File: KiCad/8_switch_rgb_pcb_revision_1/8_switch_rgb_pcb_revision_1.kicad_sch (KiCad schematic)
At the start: 95 parts, among them SW0 SW0, SW1 SW1, SW2 SW2, SW3 SW3, SW4 SW4, SW5 SW5, SW6 SW6, SW7 SW7, U2 74HC165, Y1 16MHz

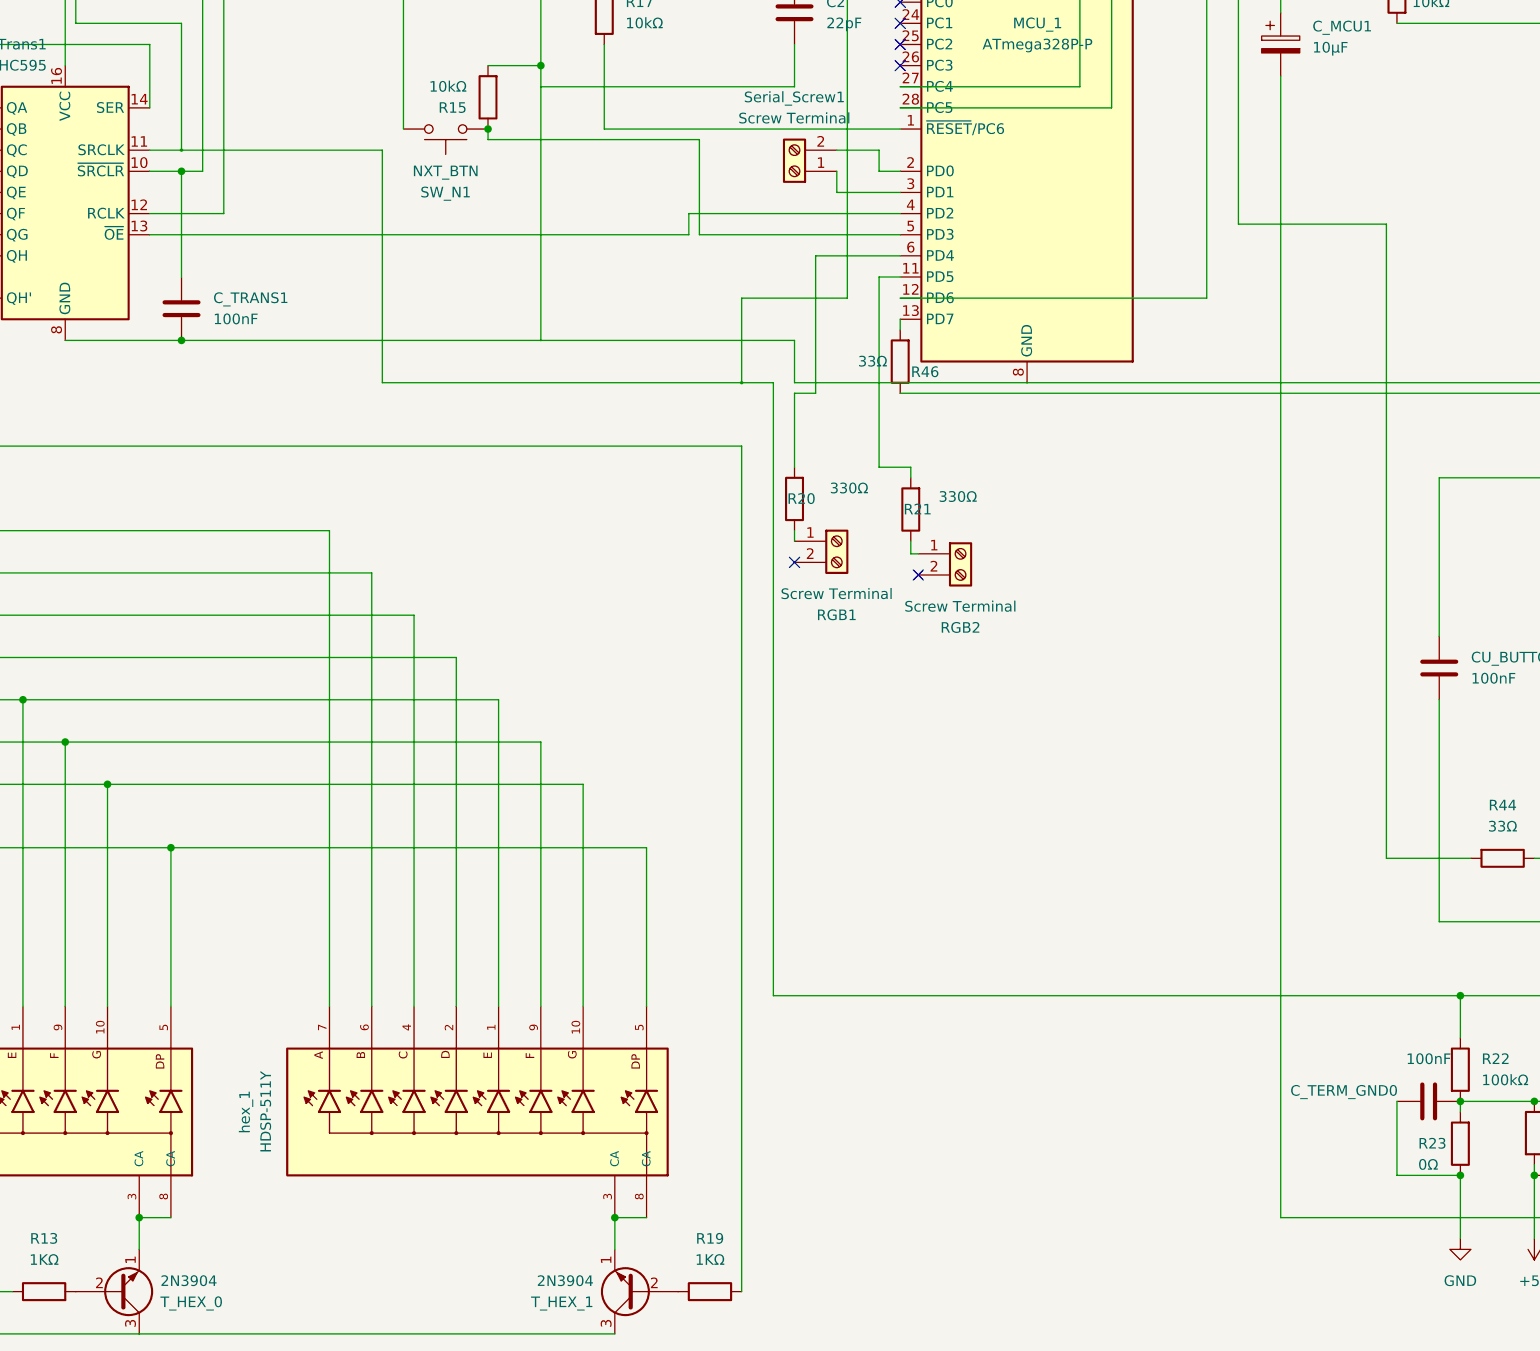
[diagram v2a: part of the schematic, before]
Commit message: Connected all traces. Will now run DRC This is the last 2-layer board with more than 10 components I ever create.
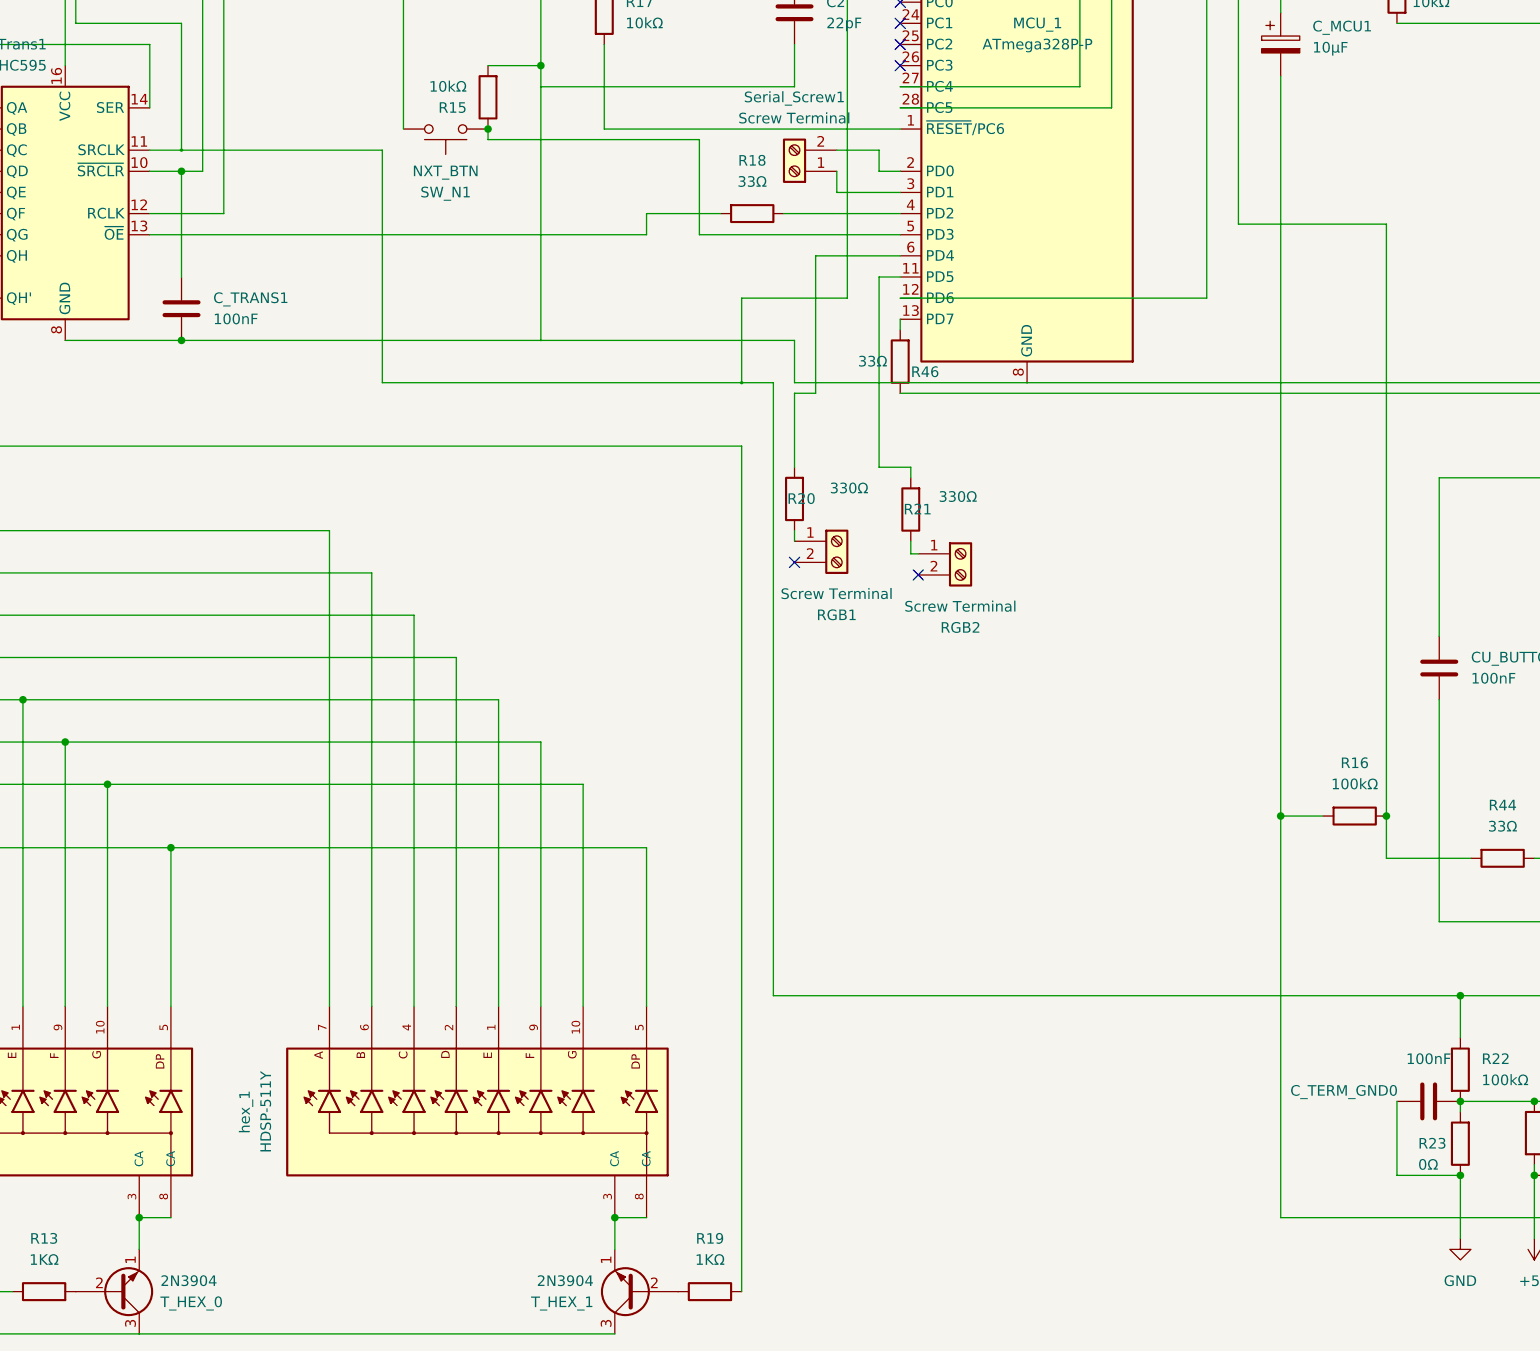
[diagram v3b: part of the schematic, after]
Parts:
- added R16: 100kΩ, Resistor_THT:R_Axial_DIN0204_L3.6mm_D1.6mm_P5.08mm_Horizontal, symbol Device:R
- added R18: 33Ω, Resistor_THT:R_Axial_DIN0204_L3.6mm_D1.6mm_P5.08mm_Horizontal, symbol Device:R
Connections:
- net GND: now also R16.2
- net at U_Trans1.13 (~{OE}): now also R18.2; no longer MCU_1.4 (PD2)
- net at MCU_1.18 (PB4), R44.2: now also R16.1
- new net: MCU_1.4 (PD2), R18.1
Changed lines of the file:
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@@
   (junction (at 134.62 170.18) (diameter 0) (color 0 0 0 0)
   )
+  (junction (at 303.53 189.23) (diameter 0) (color 0 0 0 0)
+  )
   (junction (at 66.04 165.1) (diameter 0) (color 0 0 0 0)
   )
@@
   (junction (at 398.78 175.26) (diameter 0.2) (color 0 0 0 1)
   )
+  (junction (at 290.83 189.23) (diameter 0) (color 0 0 0 0)
+  )
   (junction (at 321.31 223.52) (diameter 0) (color 0 0 0 0)
   )
@@
     (stroke (width 0) (type default))
   )
+  (wire (pts (xy 303.53 189.23) (xy 303.53 118.11))
+    (stroke (width 0) (type default))
+  )
   (wire (pts (xy 67.31 139.7) (xy 67.31 170.18))
     (stroke (width 0) (type default))
@@
     (stroke (width 0) (type default))
   )
+  (wire (pts (xy 290.83 189.23) (xy 290.83 237.49))
+    (stroke (width 0.2) (type default) (color 0 0 0 1))
+  )
   (wire (pts (xy 123.19 144.78) (xy 226.06 144.78))
     (stroke (width 0) (type default))
@@
     (stroke (width 0.2) (type default) (color 0 0 0 1))
   )
+  (wire (pts (xy 290.83 189.23) (xy 295.91 189.23))
+    (stroke (width 0.2) (type default) (color 0 0 0 1))
+  )
   (wire (pts (xy 382.27 152.4) (xy 398.78 152.4))
     (stroke (width 0.2) (type default) (color 0 0 0 1))
@@
     (stroke (width 0) (type default))
   )
-  (wire (pts (xy 303.53 194.31) (xy 303.53 118.11))
+  (wire (pts (xy 303.53 194.31) (xy 303.53 189.23))
     (stroke (width 0) (type default))
   )
@@
     (stroke (width 0.2) (type default) (color 255 0 0 1))
   )
+  (wire (pts (xy 231.14 116.84) (xy 245.11 116.84))
+    (stroke (width 0) (type default))
+  )
   (wire (pts (xy 367.03 87.63) (xy 367.03 82.55))
     (stroke (width 0) (type default))
@@
     (stroke (width 0.2) (type default) (color 255 0 0 1))
   )
-  (wire (pts (xy 219.71 116.84) (xy 245.11 116.84))
+  (wire (pts (xy 214.63 116.84) (xy 223.52 116.84))
     (stroke (width 0) (type default))
   )
@@
     (stroke (width 0) (type default))
   )
-  (wire (pts (xy 290.83 137.16) (xy 290.83 237.49))
+  (wire (pts (xy 290.83 137.16) (xy 290.83 189.23))
     (stroke (width 0.2) (type default) (color 0 0 0 1))
   )
@@
     (stroke (width 0.2) (type default) (color 255 0 0 1))
   )
-  (wire (pts (xy 219.71 119.38) (xy 219.71 116.84))
+  (wire (pts (xy 214.63 119.38) (xy 214.63 116.84))
     (stroke (width 0) (type default))
   )
@@
     (stroke (width 0) (type default))
   )
-  (wire (pts (xy 154.94 119.38) (xy 219.71 119.38))
+  (wire (pts (xy 154.94 119.38) (xy 214.63 119.38))
     (stroke (width 0) (type default))
   )
@@
     )
   )
+  (symbol (lib_id "Device:R") (at 299.72 189.23 270) (unit 1)
+    (in_bom yes) (on_board yes) (dnp no) (fields_autoplaced)
+    (property "Reference" "R16" (at 299.72 182.88 90)
+      (effects (font (size 1.27 1.27)))
+    )
+    (property "Value" "100kΩ" (at 299.72 185.42 90)
+      (effects (font (size 1.27 1.27)))
+    )
+    (property "Footprint" "Resistor_THT:R_Axial_DIN0204_L3.6mm_D1.6mm_P5.08mm_Horizontal" (at 299.72 187.452 90)
+      (effects (font (size 1.27 1.27)) hide)
+    )
+    (property "Datasheet" "~" (at 299.72 189.23 0)
+      (effects (font (size 1.27 1.27)) hide)
+    )
+    (pin "1")
+    (pin "2")
+    (instances
+      (project "8_switch_rgb_pcb_revision_1"
+        (path "/cd17c5d7-b2e9-44f9-9f0c-42378b59d72a"
+          (reference "R16") (unit 1)
+        )
+      )
+    )
+  )
   (symbol (lib_id "power:GND") (at 349.25 194.31 0) (unit 1)
     (in_bom yes) (on_board yes) (dnp no) (fields_autoplaced)
@@
         )
       )
+    )
+  )
+  (symbol (lib_id "Device:R") (at 227.33 116.84 270) (unit 1)
+    (in_bom yes) (on_board yes) (dnp no) (fields_autoplaced)
+    (property "Reference" "R18" (at 227.33 110.49 90)
+      (effects (font (size 1.27 1.27)))
+    )
+    (property "Value" "33Ω" (at 227.33 113.03 90)
+      (effects (font (size 1.27 1.27)))
+    )
+    (property "Footprint" "Resistor_THT:R_Axial_DIN0204_L3.6mm_D1.6mm_P5.08mm_Horizontal" (at 227.33 115.062 90)
+      (effects (font (size 1.27 1.27)) hide)
+    )
+    (property "Datasheet" "~" (at 227.33 116.84 0)
+      (effects (font (size 1.27 1.27)) hide)
+    )
+    (pin "1")
+    (pin "2")
+    (instances
+      (project "8_switch_rgb_pcb_revision_1"
+        (path "/cd17c5d7-b2e9-44f9-9f0c-42378b59d72a"
+          (reference "R18") (unit 1)
+        )
+      )
